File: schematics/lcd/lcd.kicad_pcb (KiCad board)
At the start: 2 copper layers, 63.7 x 45.7 mm, 27 parts, among them J1 JST_01x06, Q1 BSS138, Q2 BSS138, Q3 BSS138, Q4 BSS138, U1 NHD-C12832A1Z, U2 TLV70033_SOT23-5

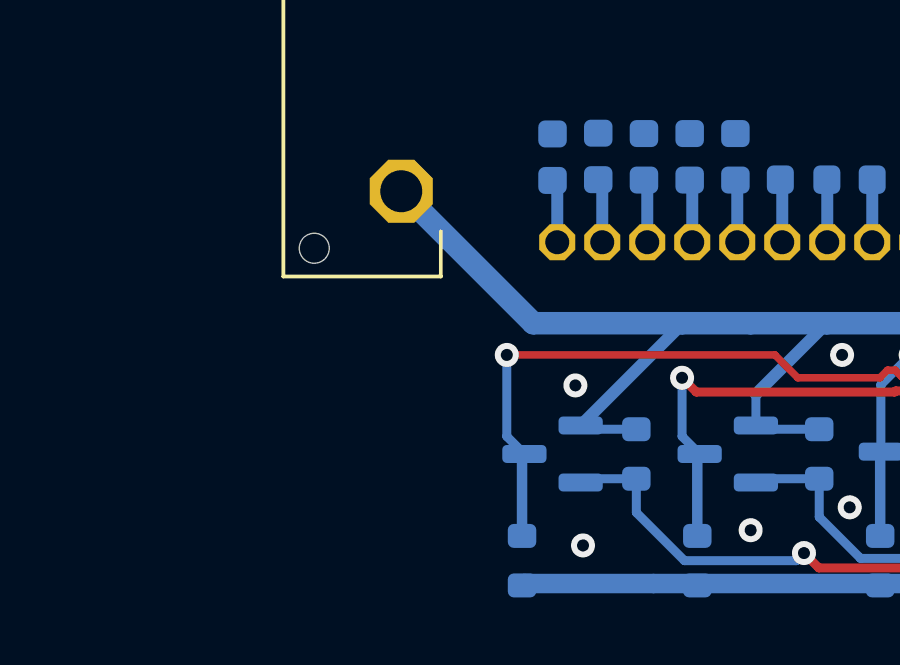
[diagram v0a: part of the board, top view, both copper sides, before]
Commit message: SCH: LCD=> add pot for backlight brightness
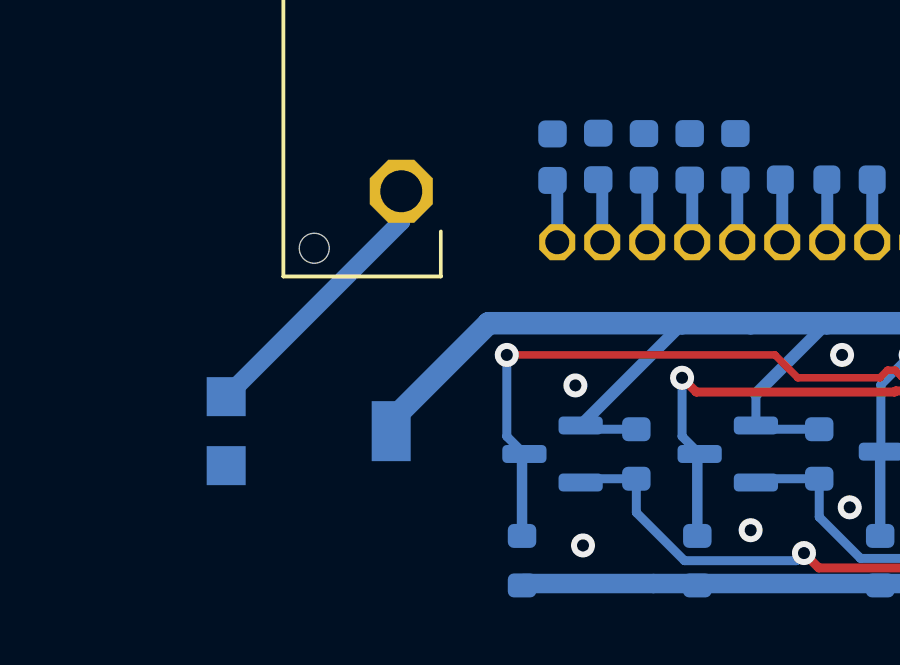
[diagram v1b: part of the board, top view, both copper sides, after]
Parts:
- added RV1: 10K, Potentiometer_SMD:Potentiometer_Bourns_3314G_Vertical, B.Cu at (76.2, 95.2)
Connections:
- U1 pad P18: +3.3V -> Net-(U1-LED+)
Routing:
- net Net-(U1-LED+): track 0.00 -> 9.26 mm
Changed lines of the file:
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@@
   (net 22 "Net-(U1-~{RST})")
   (net 23 "unconnected-(U2-NC-Pad4)")
+  (net 24 "Net-(U1-LED+)")
   (footprint "library:NHD-C12832A1Z" (layer "F.Cu")
     (at 96.106 79.594)
+    (property "JLCPCB BOM" "0")
     (property "Sheetfile" "lcd.kicad_sch")
     (property "Sheetname" "")
@@
     (pad "P18" thru_hole roundrect (at -16.82 7.66) (size 2.1 2.1) (drill 1.4) (layers "*.Cu" "*.Mask") (roundrect_rratio 0.25)
       (chamfer_ratio 0.2928932188) (chamfer top_left top_right bottom_left bottom_right)
-      (net 3 "+3.3V") (pinfunction "LED+") (pintype "power_in") (solder_mask_margin 0.0508) (thermal_bridge_angle 45))
+      (net 24 "Net-(U1-LED+)") (pinfunction "LED+") (pintype "power_in") (solder_mask_margin 0.0508) (thermal_bridge_angle 45))
     (pad "P19" thru_hole roundrect (at 17.78 7.66) (size 2.1 2.1) (drill 1.4) (layers "*.Cu" "*.Mask") (roundrect_rratio 0.25)
       (chamfer_ratio 0.2928932188) (chamfer top_left top_right bottom_left bottom_right)
@@
     (descr "SOT, 5 Pin (https://www.jedec.org/sites/default/files/docs/Mo-178c.PDF variant AA), generated with kicad-footprint-generator ipc_gullwing_generator.py")
     (tags "SOT TO_SOT_SMD")
-    (property "LCSC" "C2871194")
     (property "Sheetfile" "lcd.kicad_sch")
     (property "Sheetname" "")
     (property "ki_description" "200mA Low Dropout Voltage Regulator, Fixed Output 3.3V, SOT-23-5")
     (property "ki_keywords" "200mA LDO Regulator Fixed Positive")
+    (property "lscs" "C2871194")
     (attr smd)
     (fp_text reference "U2" (at 3.4235 1.082) (layer "B.SilkS")
@@
       (net 2 "GND") (pintype "passive"))
     (model "${KICAD6_3DMODEL_DIR}/Capacitor_SMD.3dshapes/C_0603_1608Metric.wrl"
+      (offset (xyz 0 0 0))
+      (scale (xyz 1 1 1))
+      (rotate (xyz 0 0 0))
+    )
+  )
+  (footprint "Potentiometer_SMD:Potentiometer_Bourns_3314G_Vertical" (layer "B.Cu")
+    (at 76.2 95.25 -90)
+    (descr "Potentiometer, vertical, Bourns 3314G, http://www.bourns.com/docs/Product-Datasheets/3314.pdf")
+    (tags "Potentiometer vertical Bourns 3314G")
+    (property "Sheetfile" "lcd.kicad_sch")
+    (property "Sheetname" "")
+    (property "ki_description" "Potentiometer")
+    (property "ki_keywords" "resistor variable")
+    (property "lcsc" "C780220")
+    (attr smd)
+    (fp_text reference "RV1" (at 0 4.65 90) (layer "B.SilkS")
+        (effects (font (size 1 1) (thickness 0.15)) (justify mirror))
+    )
+    (fp_text value "10K" (at 0 -4.65 90) (layer "B.Fab")
+        (effects (font (size 1 1) (thickness 0.15)) (justify mirror))
+    )
+    (fp_text user "${REFERENCE}" (at 0 1.7 90) (layer "B.Fab")
+        (effects (font (size 0.63 0.63) (thickness 0.15)) (justify mirror))
+    )
+    (fp_line (start -2.37 -2.37) (end -1.24 -2.37)
+      (stroke (width 0.12) (type solid)) (layer "B.SilkS"))
+    (fp_line (start -2.37 2.37) (end -2.37 -2.37)
+      (stroke (width 0.12) (type solid)) (layer "B.SilkS"))
+    (fp_line (start -2.37 2.37) (end -2.039 2.37)
+      (stroke (width 0.12) (type solid)) (layer "B.SilkS"))
+    (fp_line (start -0.259 2.37) (end 0.26 2.37)
+      (stroke (width 0.12) (type solid)) (layer "B.SilkS"))
+    (fp_line (start 1.24 -2.37) (end 2.37 -2.37)
+      (stroke (width 0.12) (type solid)) (layer "B.SilkS"))
+    (fp_line (start 2.04 2.37) (end 2.37 2.37)
+      (stroke (width 0.12) (type solid)) (layer "B.SilkS"))
+    (fp_line (start 2.37 2.37) (end 2.37 -2.37)
+      (stroke (width 0.12) (type solid)) (layer "B.SilkS"))
+    (fp_line (start -2.5 -3.65) (end 2.5 -3.65)
+      (stroke (width 0.05) (type solid)) (layer "B.CrtYd"))
+    (fp_line (start -2.5 3.65) (end -2.5 -3.65)
+      (stroke (width 0.05) (type solid)) (layer "B.CrtYd"))
+    (fp_line (start 2.5 -3.65) (end 2.5 3.65)
+      (stroke (width 0.05) (type solid)) (layer "B.CrtYd"))
+    (fp_line (start 2.5 3.65) (end -2.5 3.65)
+      (stroke (width 0.05) (type solid)) (layer "B.CrtYd"))
+    (fp_line (start -2.25 -2.25) (end 2.25 -2.25)
+      (stroke (width 0.1) (type solid)) (layer "B.Fab"))
+    (fp_line (start -2.25 2.25) (end -2.25 -2.25)
+      (stroke (width 0.1) (type solid)) (layer "B.Fab"))
+    (fp_line (start 0 -0.99) (end 0.001 0.989)
+      (stroke (width 0.1) (type solid)) (layer "B.Fab"))
+    (fp_line (start 0 -0.99) (end 0.001 0.989)
+      (stroke (width 0.1) (type solid)) (layer "B.Fab"))
+    (fp_line (start 2.25 -2.25) (end 2.25 2.25)
+      (stroke (width 0.1) (type solid)) (layer "B.Fab"))
+    (fp_line (start 2.25 2.25) (end -2.25 2.25)
+      (stroke (width 0.1) (type solid)) (layer "B.Fab"))
+    (fp_circle (center 0 0) (end 1 0)
+      (stroke (width 0.1) (type solid)) (fill none) (layer "B.Fab"))
+    (pad "1" smd rect (at 1.15 2.75 270) (size 1.3 1.3) (layers "B.Cu" "B.Paste" "B.Mask")
+      (net 2 "GND") (pinfunction "1") (pintype "passive"))
+    (pad "2" smd rect (at 0 -2.75 270) (size 2 1.3) (layers "B.Cu" "B.Paste" "B.Mask")
+      (net 3 "+3.3V") (pinfunction "2") (pintype "passive"))
+    (pad "3" smd rect (at -1.15 2.75 270) (size 1.3 1.3) (layers "B.Cu" "B.Paste" "B.Mask")
+      (net 24 "Net-(U1-LED+)") (pinfunction "3") (pintype "passive"))
+    (model "${KICAD6_3DMODEL_DIR}/Potentiometer_SMD.3dshapes/Potentiometer_Bourns_3314G_Vertical.wrl"
       (offset (xyz 0 0 0))
       (scale (xyz 1 1 1))
@@
   (segment (start 100.986 90.559) (end 101.105 90.678) (width 0.75) (layer "B.Cu") (net 3))
   (segment (start 108.712 80.142) (end 106.934 81.92) (width 0.75) (layer "B.Cu") (net 3))
-  (segment (start 88.646 91.653) (end 83.685 91.653) (width 0.75) (layer "B.Cu") (net 3))
   (segment (start 97.198 94.933) (end 97.1475 94.9835) (width 0.3) (layer "B.Cu") (net 3))
   (segment (start 104.902 92.202) (end 103.886 91.186) (width 0.4) (layer "B.Cu") (net 3))
@@
   (segment (start 85.3905 95.187) (end 85.2655 95.062) (width 0.3) (layer "B.Cu") (net 3))
   (segment (start 93.218 95.187) (end 91.2325 95.187) (width 0.3) (layer "B.Cu") (net 3))
-  (segment (start 83.685 91.653) (end 79.286 87.254) (width 0.75) (layer "B.Cu") (net 3))
   (segment (start 100.986 88.954) (end 100.986 86.987) (width 0.75) (layer "B.Cu") (net 3))
   (segment (start 99.314 94.933) (end 97.198 94.933) (width 0.3) (layer "B.Cu") (net 3))
   (segment (start 100.986 88.954) (end 100.986 90.559) (width 0.75) (layer "B.Cu") (net 3))
   (segment (start 91.2325 95.187) (end 91.1075 95.062) (width 0.3) (layer "B.Cu") (net 3))
+  (segment (start 82.197 91.653) (end 78.95 94.9) (width 0.75) (layer "B.Cu") (net 3))
   (segment (start 96.587859 91.653) (end 93.472 91.653) (width 0.75) (layer "B.Cu") (net 3))
   (segment (start 90.932 91.653) (end 88.646 91.653) (width 0.75) (layer "B.Cu") (net 3))
   (segment (start 106.934 81.92) (end 106.934 85.726) (width 0.75) (layer "B.Cu") (net 3))
   (segment (start 100.986 86.987) (end 101.105 86.868) (width 0.75) (layer "B.Cu") (net 3))
+  (segment (start 88.646 91.653) (end 82.197 91.653) (width 0.75) (layer "B.Cu") (net 3))
   (segment (start 85.2655 95.062) (end 88.646 91.6815) (width 0.4) (layer "B.Cu") (net 3))
   (segment (start 104.902 94.933) (end 104.902 92.202) (width 0.4) (layer "B.Cu") (net 3))
@@
   (segment (start 97.1475 94.6355) (end 100.13 91.653) (width 0.4) (layer "B.Cu") (net 3))
   (segment (start 87.122 95.187) (end 85.3905 95.187) (width 0.3) (layer "B.Cu") (net 3))
+  (segment (start 78.95 94.9) (end 78.95 95.25) (width 0.75) (layer "B.Cu") (net 3))
   (segment (start 100.625 91.653) (end 100.33 91.948) (width 0.75) (layer "B.Cu") (net 3))
   (segment (start 103.886 91.186) (end 101.092 91.186) (width 0.4) (layer "B.Cu") (net 3))
@@
   (segment (start 106.986 88.954) (end 106.986 87.428) (width 0.4) (layer "B.Cu") (net 22))
   (segment (start 106.986 87.428) (end 106.934 87.376) (width 0.25) (layer "B.Cu") (net 22))
+  (segment (start 73.45 94.1) (end 79.286 88.264) (width 0.6) (layer "B.Cu") (net 24))
+  (segment (start 79.286 88.264) (end 79.286 87.254) (width 0.6) (layer "B.Cu") (net 24))
   (zone (net 2) (net_name "GND") (layer "F.Cu") (hatch edge 0.5)
     (connect_pads (clearance 0.5))

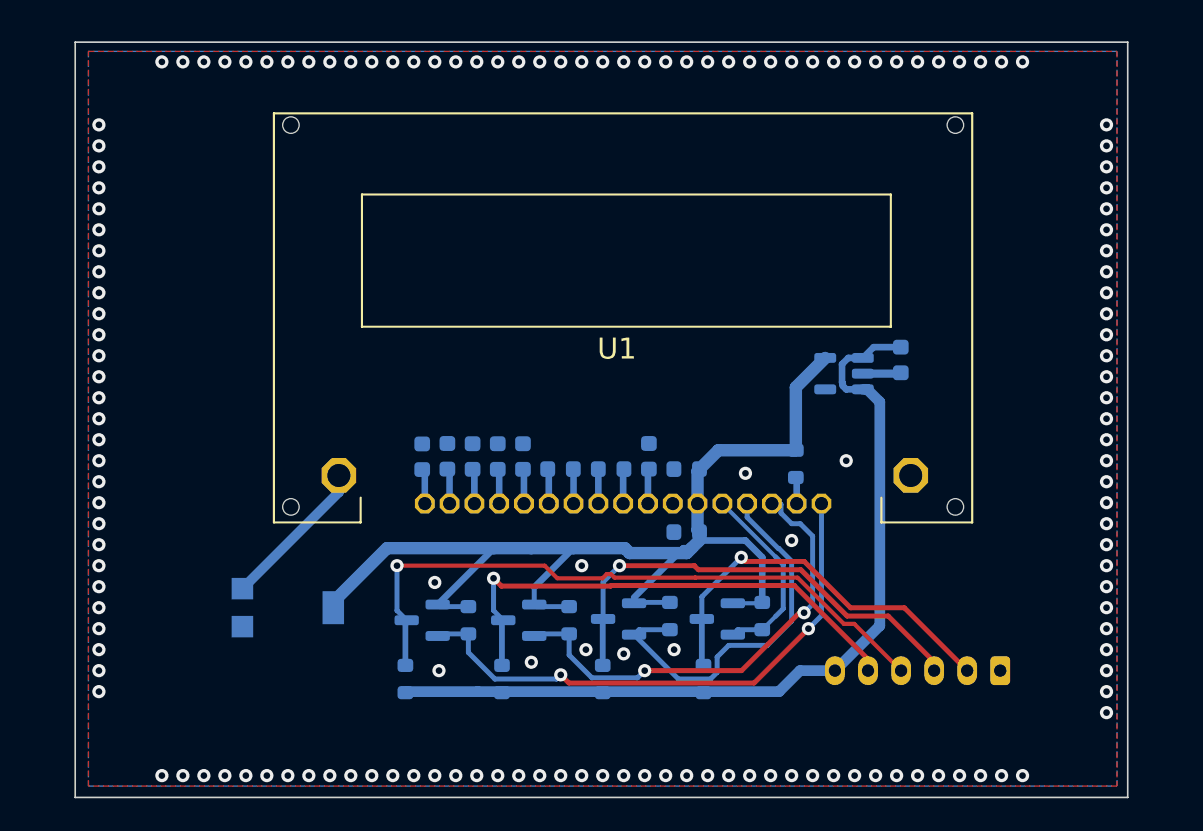
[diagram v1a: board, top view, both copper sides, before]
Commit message: SCH: LCD=> Changed level shifter
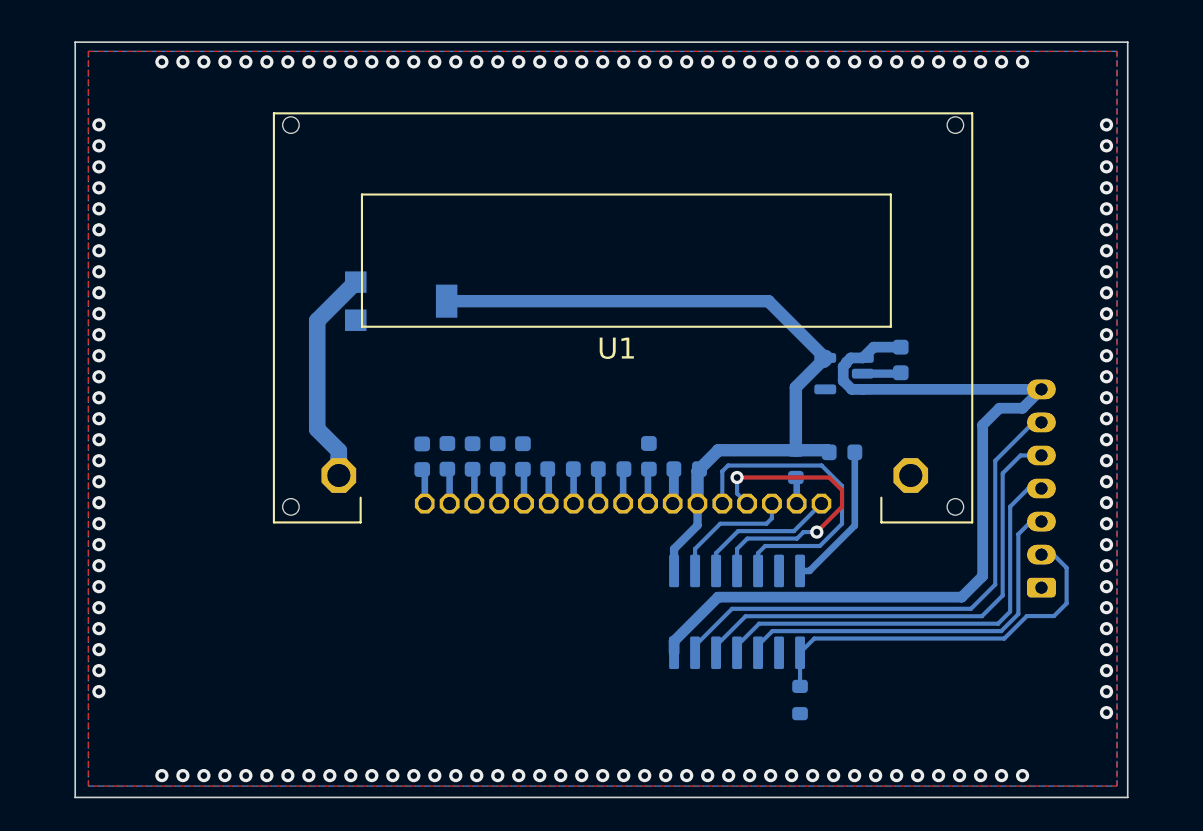
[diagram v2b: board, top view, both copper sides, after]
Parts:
- removed Q1, Q2, Q3, Q4: BSS138, Package_TO_SOT_SMD:SOT-23
- removed R3, R4, R5, R6, R7, R8, R9: 10K, Resistor_SMD:R_0603_1608Metric
- added U3: TXS0104EDR, library:SOIC127P600X175-14N, B.Cu at (103.4, 95.5)
- J1: value JST_01x06 -> Conn_01x07_Socket; footprint Connector_JST:JST_PH_B6B-PH-K_1x06_P2.00mm_Vertical -> Connector_JST:JST_PH_B7B-PH-K_1x07_P2.00mm_Vertical
- moved R2 20.6 mm to (107.2, 100.8), turned to 90 degrees
- moved RV1 19.8 mm to (83.1, 76.7)
- moved C3 10.6 mm to (109.7, 85.9), turned to 0 degrees
- moved J1 5.60 mm to (121.8, 94.0), turned to 90 degrees
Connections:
- J1 pad 2: /MCU_SDA -> /MCU_OE
- J1 pad 3: /MCU_SCL -> /MCU_SDA
- J1 pad 4: /MCU_CS -> /MCU_SCL
- J1 pad 5: /MCU_A0 -> /MCU_CS
- J1 pad 6: +5V -> /MCU_A0
- R2 pad 1: +3.3V -> GND
- R2 pad 2: /LCD_CS -> /MCU_OE
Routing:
- net +3.3V: track 71.7 -> 46.0 mm
- net /LCD_CS: track 33.8 -> 8.70 mm, vias 2 -> 0
- net /MCU_OE: track 0.00 -> 23.4 mm
- net /LCD_A0: track 28.3 -> 7.64 mm, vias 2 -> 0
- net GND: track 2.51 -> 13.4 mm, vias 151 -> 141
- net /MCU_CS: track 39.6 -> 29.2 mm, vias 1 -> 0
- net /LCD_SDA: track 11.6 -> 19.0 mm
- net Net-(U1-LED+): track 9.26 -> 14.3 mm
- net /LCD_SCL: track 23.2 -> 18.2 mm, vias 0 -> 2
- net /MCU_SCL: track 28.4 -> 26.5 mm, vias 1 -> 0
- net /MCU_A0: track 31.0 -> 31.4 mm, vias 1 -> 0
- net /MCU_SDA: track 24.1 -> 23.7 mm, vias 1 -> 0

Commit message: SCH: LCD=> fixes, production ready
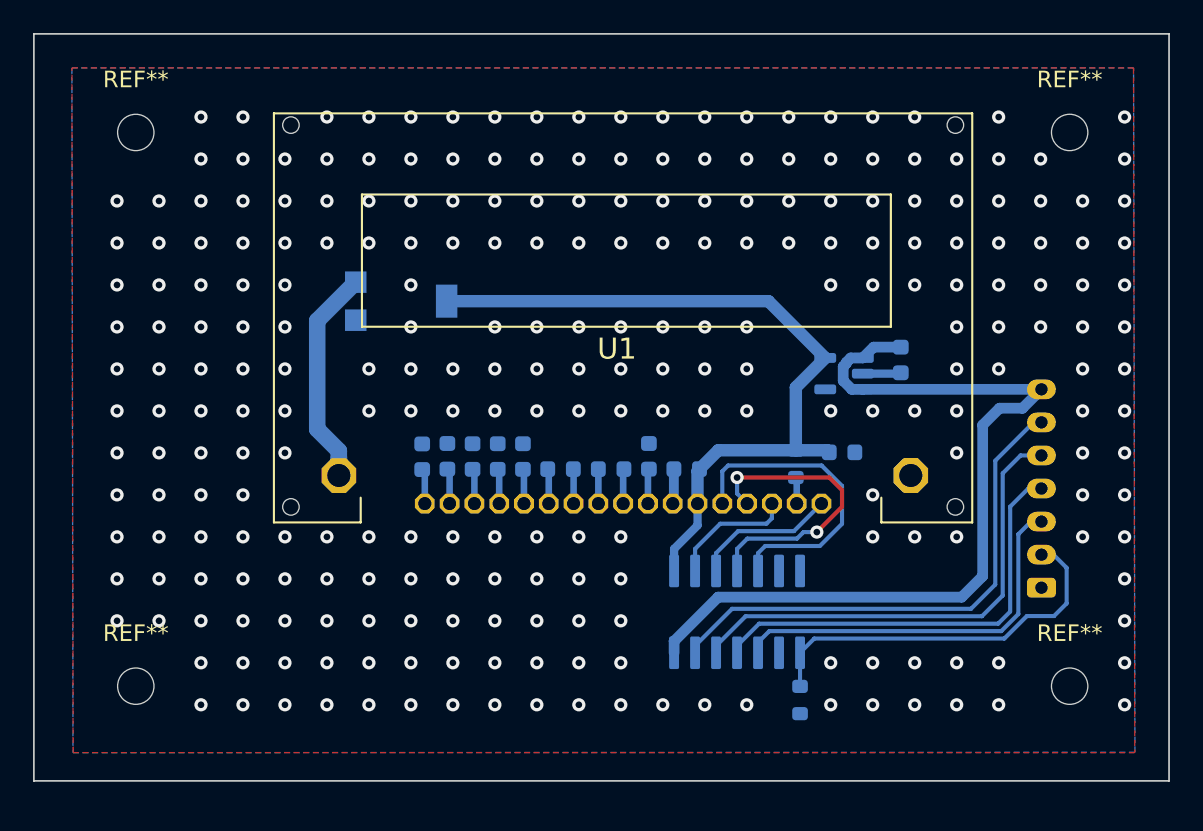
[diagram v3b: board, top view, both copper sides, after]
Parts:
- added REF**: MountingHole_2.2mm_M2, MountingHole:MountingHole_2.2mm_M2, F.Cu at (67.0, 100.0)
- added REF**: MountingHole_2.2mm_M2, MountingHole:MountingHole_2.2mm_M2, F.Cu at (67.0, 66.5)
- added REF**: MountingHole_2.2mm_M2, MountingHole:MountingHole_2.2mm_M2, F.Cu at (123.5, 66.5)
- added REF**: MountingHole_2.2mm_M2, MountingHole:MountingHole_2.2mm_M2, F.Cu at (123.5, 100.0)
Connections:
- net Net-(U1-LED+) renamed VD
- U3 pad 6: unconnected-(U3-NC-Pad6) -> (no net)
- U3 pad 9: unconnected-(U3-NC-Pad9) -> (no net)
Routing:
- net GND: track 13.4 -> 4.53 mm, vias 141 -> 261
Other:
- board size 63.7 x 45.7 mm -> 68.7 x 45.2 mm
